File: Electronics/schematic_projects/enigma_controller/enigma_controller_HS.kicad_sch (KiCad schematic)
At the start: 29 parts, among them IC11 RT9742SNGV, IC12 TPD1E05U06DPYT, IC13 ESD224DQAR, IC14 ESD224DQAR, IC4 ESD321DYAR, IC5 ESD321DYAR, IC6 ESD321DYAR, IC7 ESD321DYAR, IC8 AP22653W6-7, J10 A70-112-331N126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

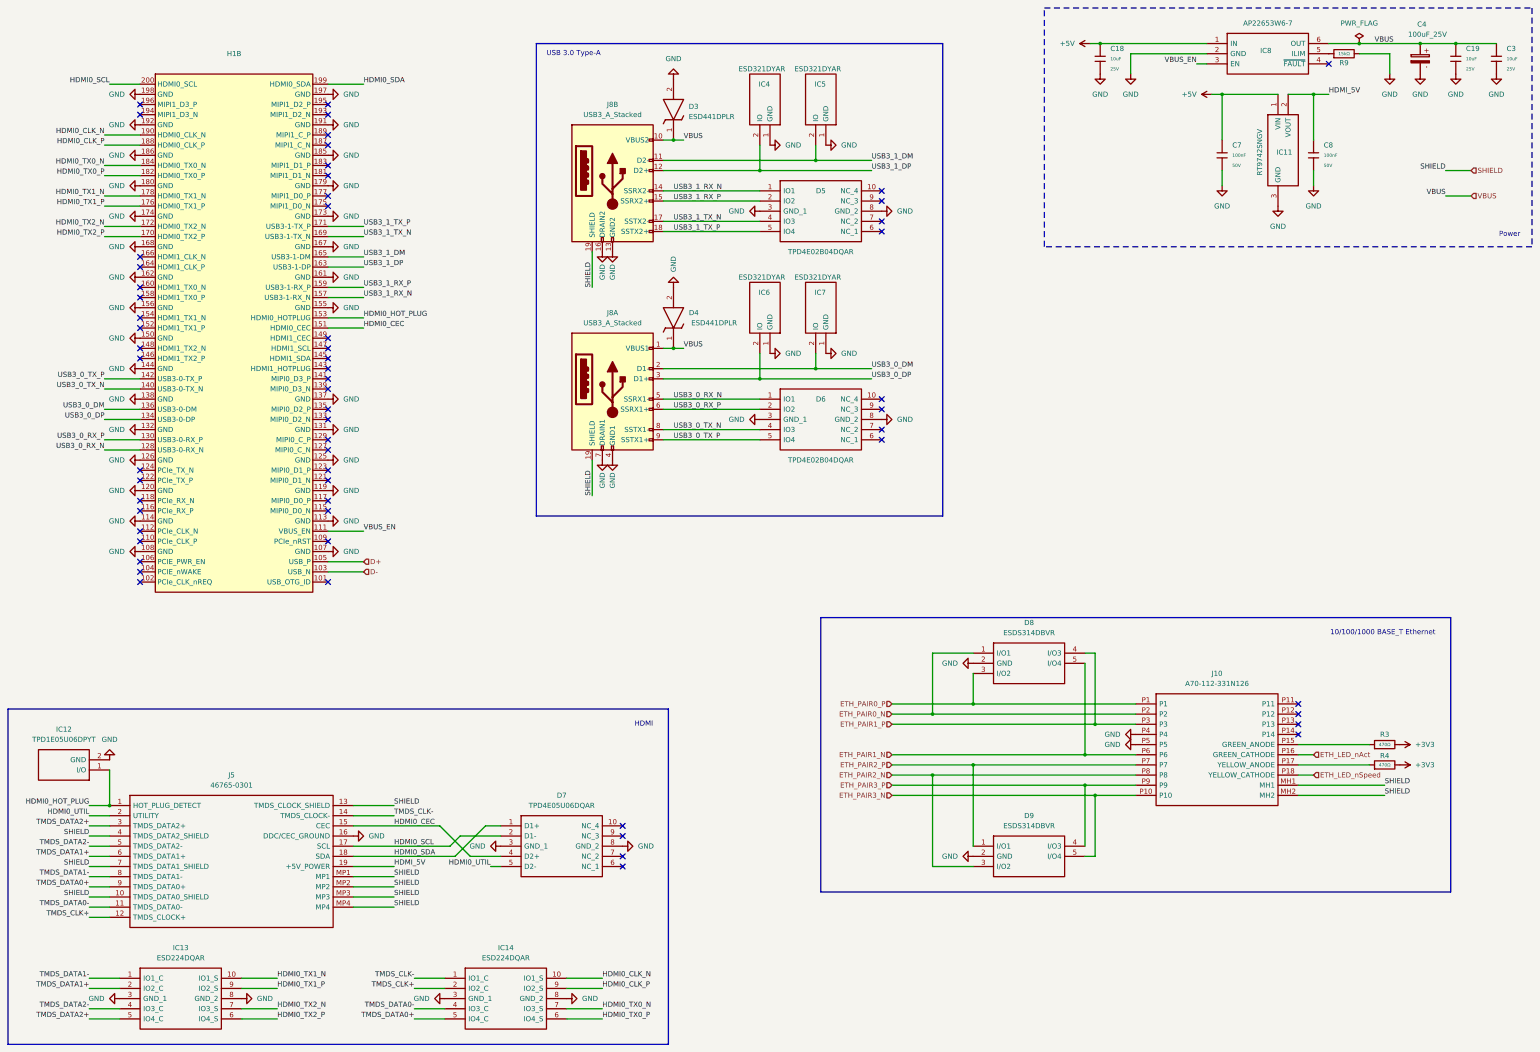
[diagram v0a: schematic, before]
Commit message: Updated for impedance calculated trace widths.
Also added slow signals and traces for ESD protection components.
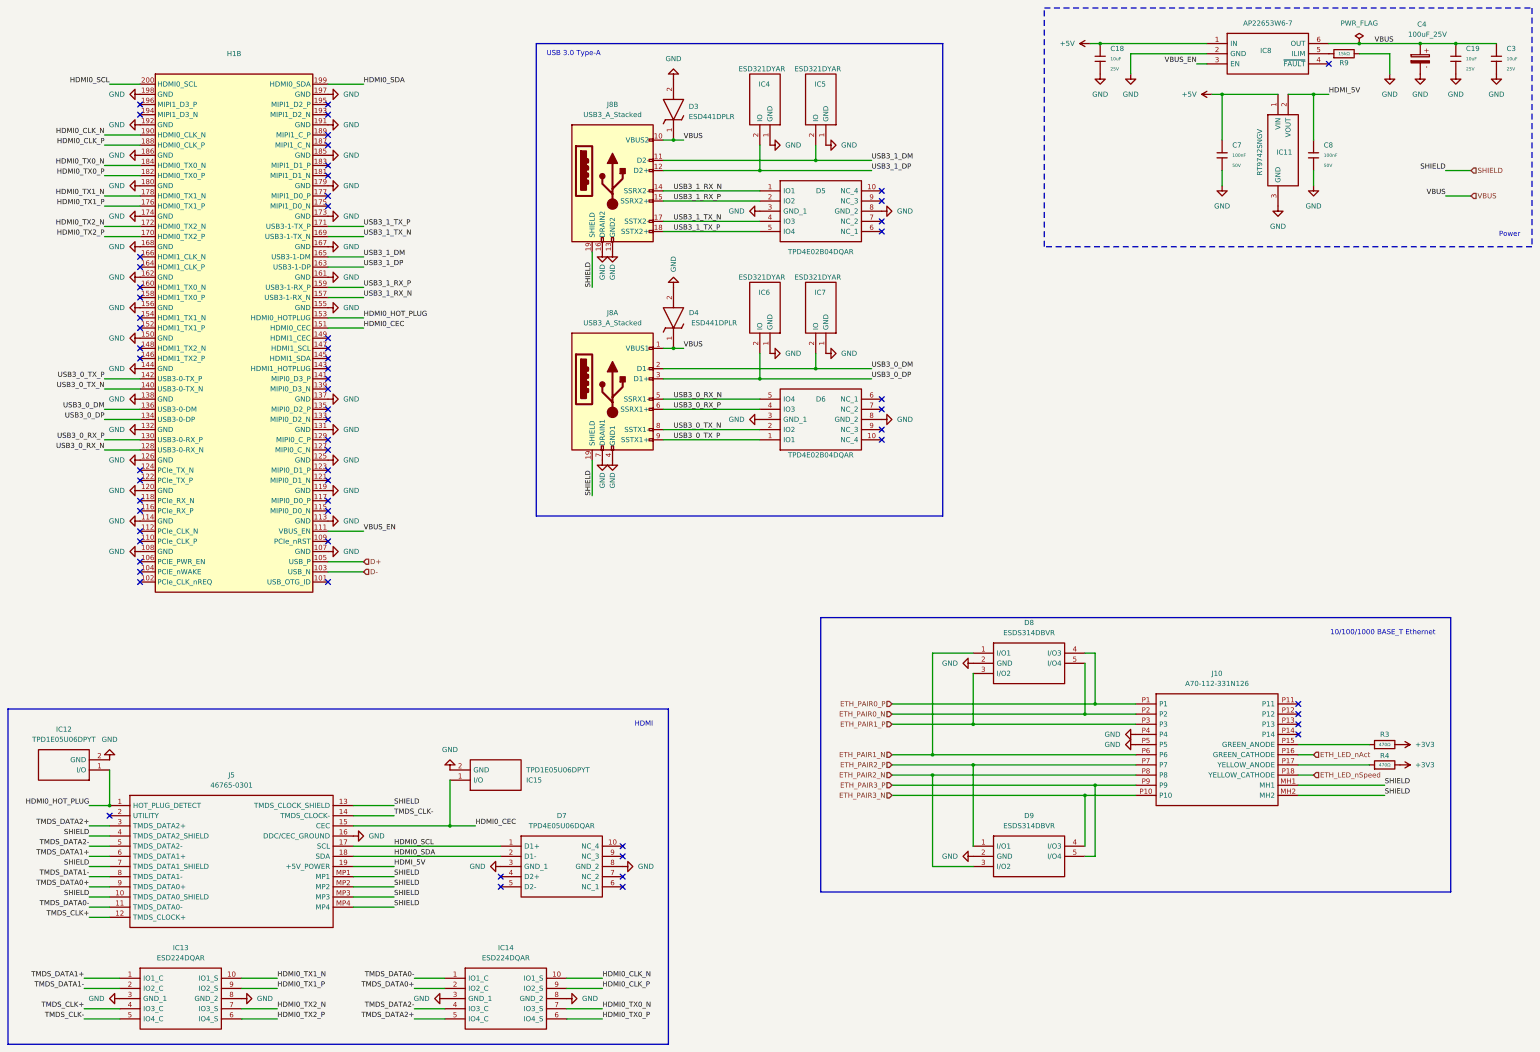
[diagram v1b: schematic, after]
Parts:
- added IC15: TPD1E05U06DPYT, Enigma_Components:TPD1E05U06DPYT, symbol Enigma_Components:TPD1E05U06DPYT
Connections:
- net ETH_PAIR0_N: now also D8.5 (I/O4); no longer D8.1 (I/O1)
- net ETH_PAIR0_P: now also D8.4 (I/O3); no longer D8.3 (I/O2)
- net ETH_PAIR1_N: now also D8.1 (I/O1); no longer D8.5 (I/O4)
- net ETH_PAIR1_P: now also D8.3 (I/O2); no longer D8.4 (I/O3)
- net ETH_PAIR3_N: now also D9.4 (I/O3); no longer D9.5 (I/O4)
- net ETH_PAIR3_P: now also D9.5 (I/O4); no longer D9.4 (I/O3)
- net GND: now also IC15.2 (GND)
- net HDMI0_CEC: now also IC15.1 (I/O); no longer D7.4 (D2+)
- net HDMI0_SCL: now also D7.1 (D1+); no longer D7.2 (D1-)
- net HDMI0_SDA: now also D7.2 (D1-); no longer D7.1 (D1+)
- net TMDS_CLK+: now also IC13.4 (IO3_C); no longer IC14.2 (IO2_C)
- net TMDS_CLK-: now also IC13.5 (IO4_C); no longer IC14.1 (IO1_C)
- net TMDS_DATA0+: now also IC14.2 (IO2_C); no longer IC14.5 (IO4_C)
- net TMDS_DATA0-: now also IC14.1 (IO1_C); no longer IC14.4 (IO3_C)
- net TMDS_DATA1+: now also IC13.1 (IO1_C); no longer IC13.2 (IO2_C)
- net TMDS_DATA1-: now also IC13.2 (IO2_C); no longer IC13.1 (IO1_C)
- net TMDS_DATA2+: now also IC14.5 (IO4_C); no longer IC13.5 (IO4_C)
- net TMDS_DATA2-: now also IC14.4 (IO3_C); no longer IC13.4 (IO3_C)
- net USB3_0_RX_N: now also D6.5 (IO4); no longer D6.1 (IO1)
- net USB3_0_RX_P: now also D6.4 (IO3); no longer D6.2 (IO2)
- net USB3_0_TX_N: now also D6.2 (IO2); no longer D6.4 (IO3)
- net USB3_0_TX_P: now also D6.1 (IO1); no longer D6.5 (IO4)
- net HDMI0_UTIL: no longer names the net of J5.2 (UTILITY)
- net HDMI0_UTIL: no longer D7.5 (D2-)
- no-connect marks 60 -> 63
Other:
- moved on the sheet: D7

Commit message: Added library from CM5IO reference design.
Updated high-speed traces with serpentines. Also added ground pour around high-speed lines.
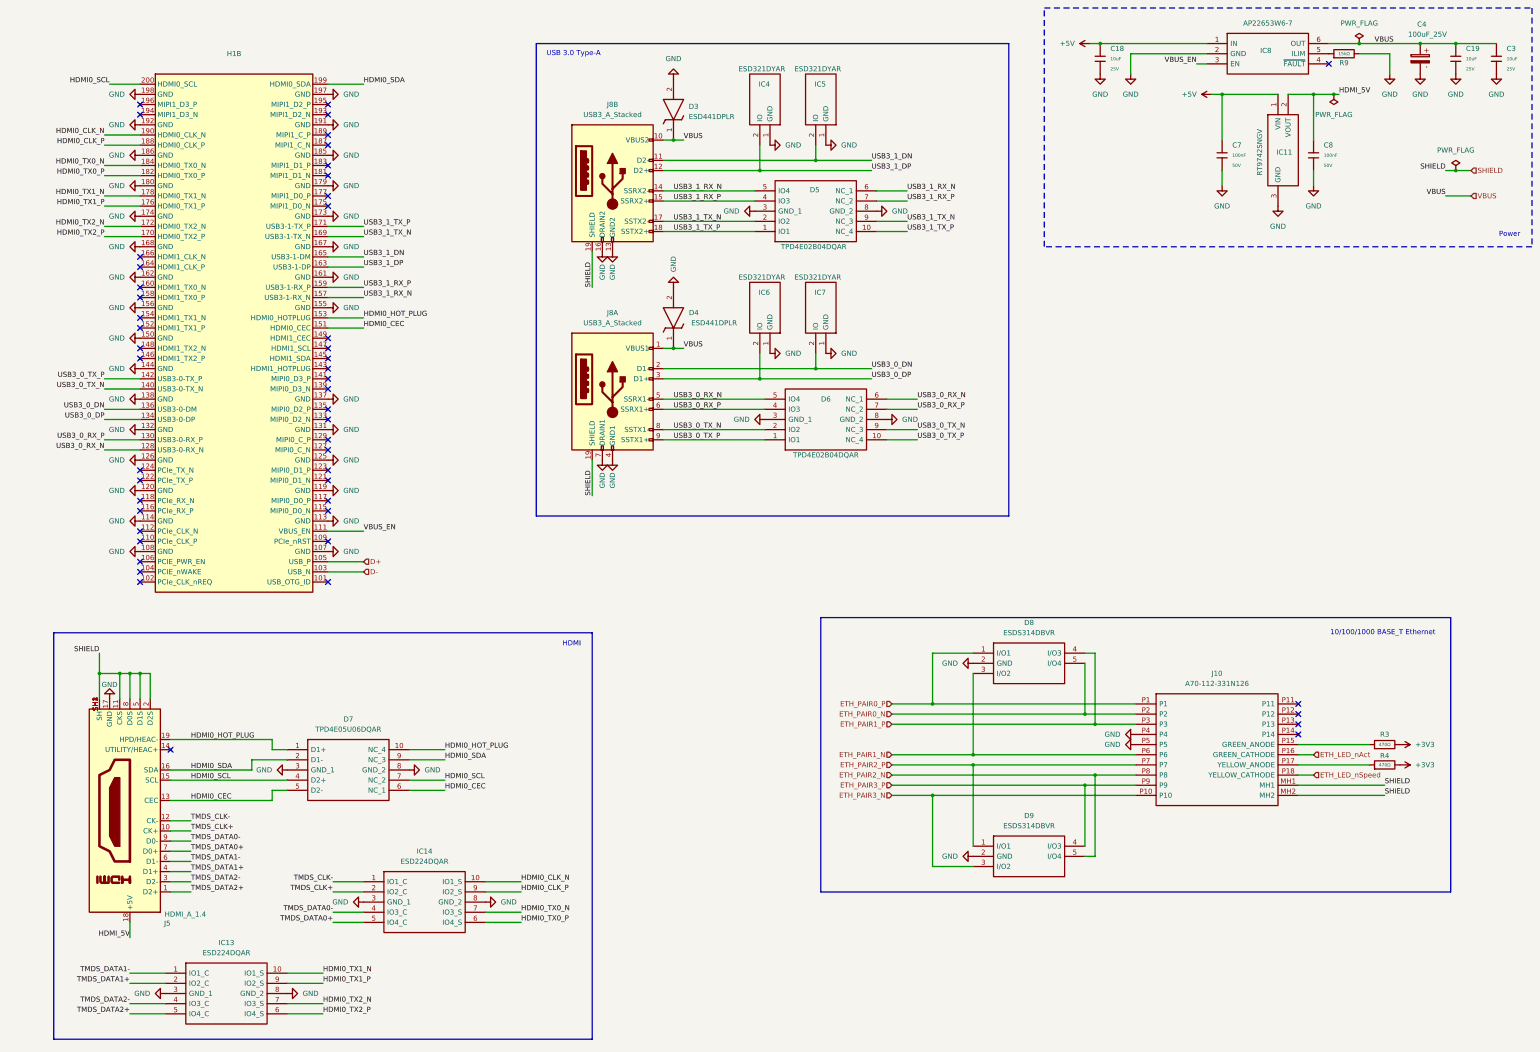
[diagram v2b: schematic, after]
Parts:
- removed IC12, IC15: TPD1E05U06DPYT, Enigma_Components:TPD1E05U06DPYT, symbol Enigma_Components:TPD1E05U06DPYT
- removed J5: 46765-0301, Enigma_Components:467650301, symbol Enigma_Components:46765-0301
- added J5: HDMI_A_1.4, CM5IO:EDAC 690-019-298-412, symbol CM5IO:HDMI_A_1.4
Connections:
- net ETH_PAIR0_P: now also D8.1 (I/O1); no longer D8.4 (I/O3)
- net ETH_PAIR1_N: now also D8.3 (I/O2); no longer D8.1 (I/O1)
- net ETH_PAIR1_P: now also D8.4 (I/O3); no longer D8.3 (I/O2)
- net ETH_PAIR2_N: now also D9.5 (I/O4); no longer D9.3 (I/O2)
- net ETH_PAIR3_N: now also D9.3 (I/O2); no longer D9.4 (I/O3)
- net ETH_PAIR3_P: now also D9.4 (I/O3); no longer D9.5 (I/O4)
- net GND: now also J5.17 (GND)
- net HDMI0_CEC: now also D7.5 (D2-), D7.6 (NC_1), J5.13 (CEC)
- net HDMI0_HOT_PLUG: now also D7.1 (D1+), D7.10 (NC_4), J5.19 (HPD/HEAC-)
- net HDMI0_SCL: now also D7.4 (D2+), D7.7 (NC_2), J5.15 (SCL); no longer D7.1 (D1+)
- net HDMI0_SDA: now also D7.9 (NC_3), J5.16 (SDA)
- net HDMI_5V: now also J5.18 (+5V)
- net SHIELD: now also J5.11 (CKS), J5.2 (D2S), J5.5 (D1S), J5.8 (D0S), J5.SH1 (SH), J5.SH2 (SH), J5.SH3 (SH), J5.SH4 (SH)
- net TMDS_CLK+: now also IC14.2 (IO2_C), J5.10 (CK+); no longer IC13.4 (IO3_C)
- net TMDS_CLK-: now also IC14.1 (IO1_C), J5.12 (CK-); no longer IC13.5 (IO4_C)
- net TMDS_DATA0+: now also IC14.5 (IO4_C), J5.7 (D0+); no longer IC14.2 (IO2_C)
- net TMDS_DATA0-: now also IC14.4 (IO3_C), J5.9 (D0-); no longer IC14.1 (IO1_C)
- net TMDS_DATA1+: now also IC13.2 (IO2_C), J5.4 (D1+); no longer IC13.1 (IO1_C)
- net TMDS_DATA1-: now also IC13.1 (IO1_C), J5.6 (D1-); no longer IC13.2 (IO2_C)
- net TMDS_DATA2+: now also IC13.5 (IO4_C), J5.1 (D2+); no longer IC14.5 (IO4_C)
- net TMDS_DATA2-: now also IC13.4 (IO3_C), J5.3 (D2-); no longer IC14.4 (IO3_C)
- net USB3_0_RX_N: now also D6.6 (NC_1)
- net USB3_0_RX_P: now also D6.7 (NC_2)
- net USB3_0_TX_N: now also D6.9 (NC_3)
- net USB3_0_TX_P: now also D6.10 (NC_4)
- net USB3_1_RX_N: now also D5.5 (IO4), D5.6 (NC_1); no longer D5.1 (IO1)
- net USB3_1_RX_P: now also D5.4 (IO3), D5.7 (NC_2); no longer D5.2 (IO2)
- net USB3_1_TX_N: now also D5.2 (IO2), D5.9 (NC_3); no longer D5.4 (IO3)
- net USB3_1_TX_P: now also D5.1 (IO1), D5.10 (NC_4); no longer D5.5 (IO4)
- net USB3_0_DM renamed USB3_0_DN
- net USB3_1_DM renamed USB3_1_DN
- no-connect marks 63 -> 49
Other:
- moved on the sheet: D5, D6, D7, IC13, IC14

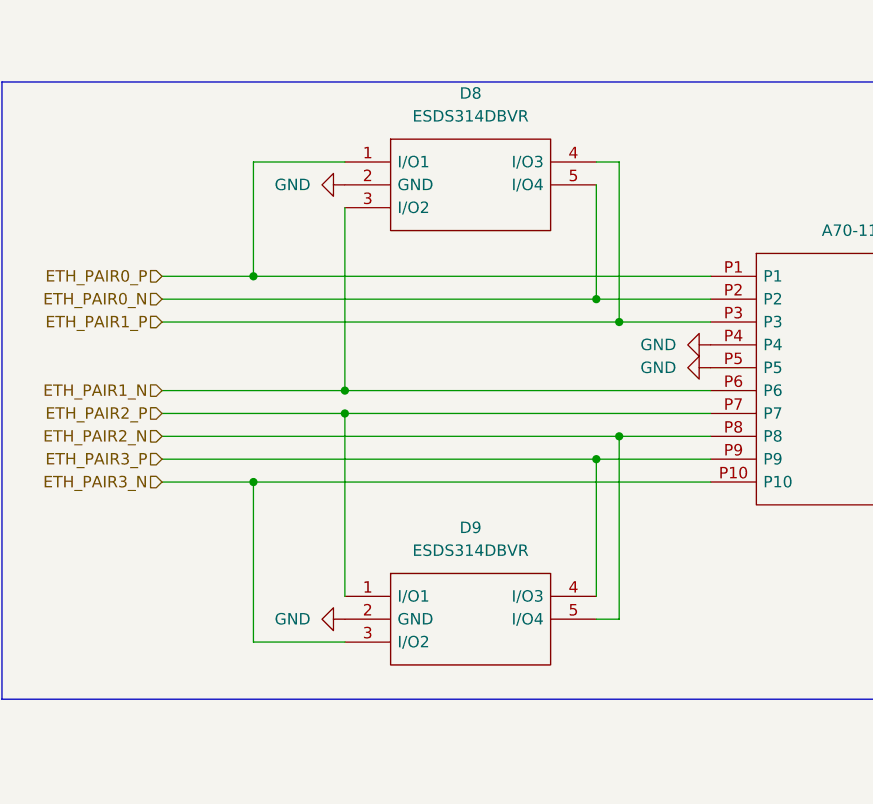
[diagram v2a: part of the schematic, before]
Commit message: Updated for new battery holder.
Also updated 3d models for components and fixed skew and trace lengths for main high-speed lines.
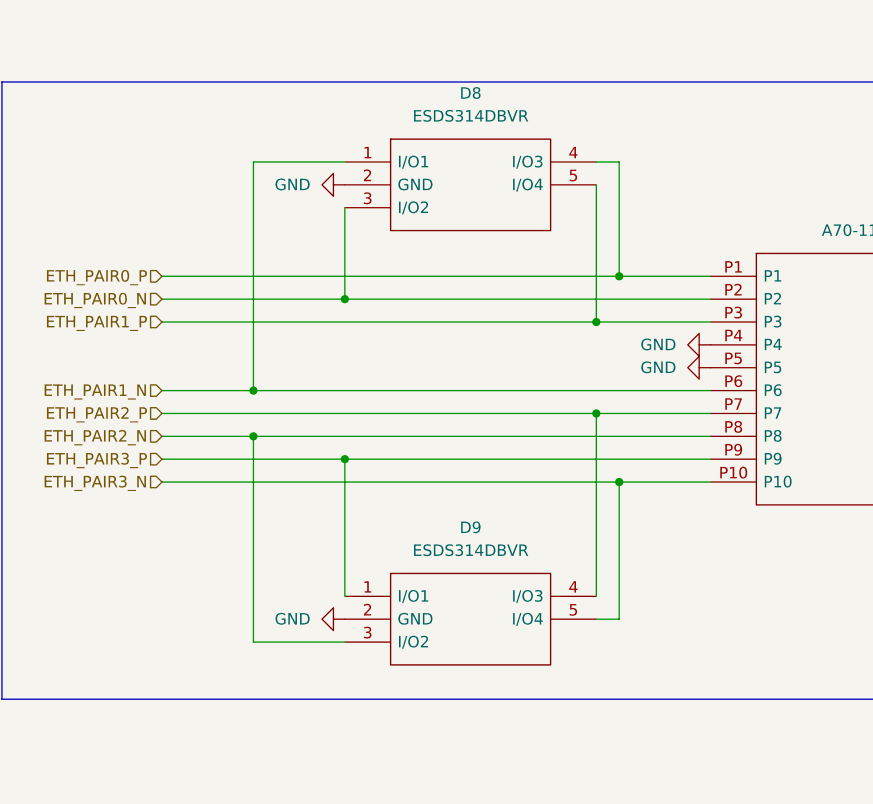
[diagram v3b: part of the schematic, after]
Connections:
- net ETH_PAIR0_N: now also D8.3 (I/O2); no longer D8.5 (I/O4)
- net ETH_PAIR0_P: now also D8.4 (I/O3); no longer D8.1 (I/O1)
- net ETH_PAIR1_N: now also D8.1 (I/O1); no longer D8.3 (I/O2)
- net ETH_PAIR1_P: now also D8.5 (I/O4); no longer D8.4 (I/O3)
- net ETH_PAIR2_N: now also D9.3 (I/O2); no longer D9.5 (I/O4)
- net ETH_PAIR2_P: now also D9.4 (I/O3); no longer D9.1 (I/O1)
- net ETH_PAIR3_N: now also D9.5 (I/O4); no longer D9.3 (I/O2)
- net ETH_PAIR3_P: now also D9.1 (I/O1); no longer D9.4 (I/O3)
